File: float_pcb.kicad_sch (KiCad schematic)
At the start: 74 parts, among them J1 Switch, J2 Conn_01x04, J3 USB_C, J4 Conn_01x03, J5 I2C, J6 Light, J7 Batt, J9 I2C, Q1 AO3400A, Q2 AO3400A, U1 TPSM863252, U2 TPSM863252, U3 USBLC6-2SC6, U4 ESP32-S3-WROOM-1, U5 USBLC6-4SC6, U6 USBLC6-4SC6

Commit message: More progress on V4
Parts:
- U4: value ESP32-S3-WROOM-1 -> ESP32-S3-WROOM-1U
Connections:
- net USBC_D+: now reaches J3.A6 (D+), J3.B6 (D+), U3.6 (I/O1)
- net USBC_D-: now reaches J3.A7 (D-), J3.B7 (D-), U3.4 (I/O2)
- net ESP32_D-: now reaches U3.3 (I/O2), U4.13 (USB_D-)
- net ESP32_D+: now reaches U3.1 (I/O1), U4.14 (USB_D+)
- net VBUS renamed VBUS_USB
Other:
- note added: "GPIO47/48 valid only for non-R16V module variants"
- note added: "USBC"
- moved on the sheet: BOOT1, J3, R10, R11, TP9, U3

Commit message: V4
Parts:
- removed J2: Conn_01x04, Connector_PinHeader_2.54mm:PinHeader_1x04_P2.54mm_Vertical, symbol Connector_Generic:Conn_01x04
- removed LS1: AT-1127-ST-2-R, buzzer:XDCR_AT-1127-ST-2-R, symbol Buzzer:AT-1127-ST-2-R
- removed Q2: AO3400A, Package_TO_SOT_SMD:SOT-23, symbol Transistor_FET:AO3400A
- removed R26: TBD, Resistor_SMD:R_0603_1608Metric, symbol Device:R
- removed U3: USBLC6-2SC6, Package_TO_SOT_SMD:SOT-23-6, symbol Power_Protection:USBLC6-2SC6
- removed U5, U6: USBLC6-4SC6, Package_TO_SOT_SMD:SOT-23-6, symbol Power_Protection:USBLC6-4SC6
- added D4, D5, D6: ESDS314, Package_TO_SOT_SMD:SOT-23-5, symbol float_pcb_symbols:ESDS314
- added H4: MH, MountingHole:MountingHole_2.2mm_M2, symbol Mechanical:MountingHole
- added J2: Conn_01x05, Connector_PinHeader_2.54mm:PinHeader_1x05_P2.54mm_Vertical, symbol Connector_Generic:Conn_01x05
- added LS1: CPT-9019A-SMT-TR, buzzer:CPT-9019A_CUD, symbol Buzzer:CPT-9019A-SMT-TR
- R20: value 10k -> 1k
- TP7: value SDA2 -> SDA1
- renumbered R25 to R22, R22 to R25
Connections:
- net ESP32_D+ is gone; now on net USBC_D+: U4.14 (USB_D+)
- net ESP32_D- is gone; now on net USBC_D-: U4.13 (USB_D-)
- net BUZZER: now also R20.1; no longer R20.2
- net GND: now also R17.1, D4.2 (GND), D5.2 (GND), D6.2 (GND), J2.5 (Pin_5), LS1.2; no longer R17.2, R20.1
- net LIGHT: now also R17.2; no longer R17.1
- net MISC1: now also R25.1, U4.33 (IO40), D5.5 (IO4), J2.1 (Pin_1); no longer R22.2, U4.32 (IO39)
- net MISC2: now also R23.1, U4.34 (IO41), D5.4 (IO3), J2.2 (Pin_2); no longer R24.2, U4.31 (IO38)
- net MISC3: now also R24.2, U4.31 (IO38), D5.3 (IO2), J2.3 (Pin_3); no longer R23.1, U4.34 (IO41)
- net MISC4: now also R22.2, U4.32 (IO39), D5.1 (IO1), J2.4 (Pin_4); no longer R25.1, U4.33 (IO40)
- net SCL1: now also D6.1 (IO1)
- net SCL2: now also D6.4 (IO3)
- net SDA1: now also D6.3 (IO2)
- net SDA2: now also D6.5 (IO4)
- net USBC_D+: now also D4.3 (IO2)
- net USBC_D-: now also D4.1 (IO1)
- net VBUS_USB renamed USB_VBUS
- new net: LS1.1, R20.2
- no-connect marks 26 -> 28
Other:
- moved on the sheet: H1, H2, H3, R17, R20, R22, R23, R24, R25

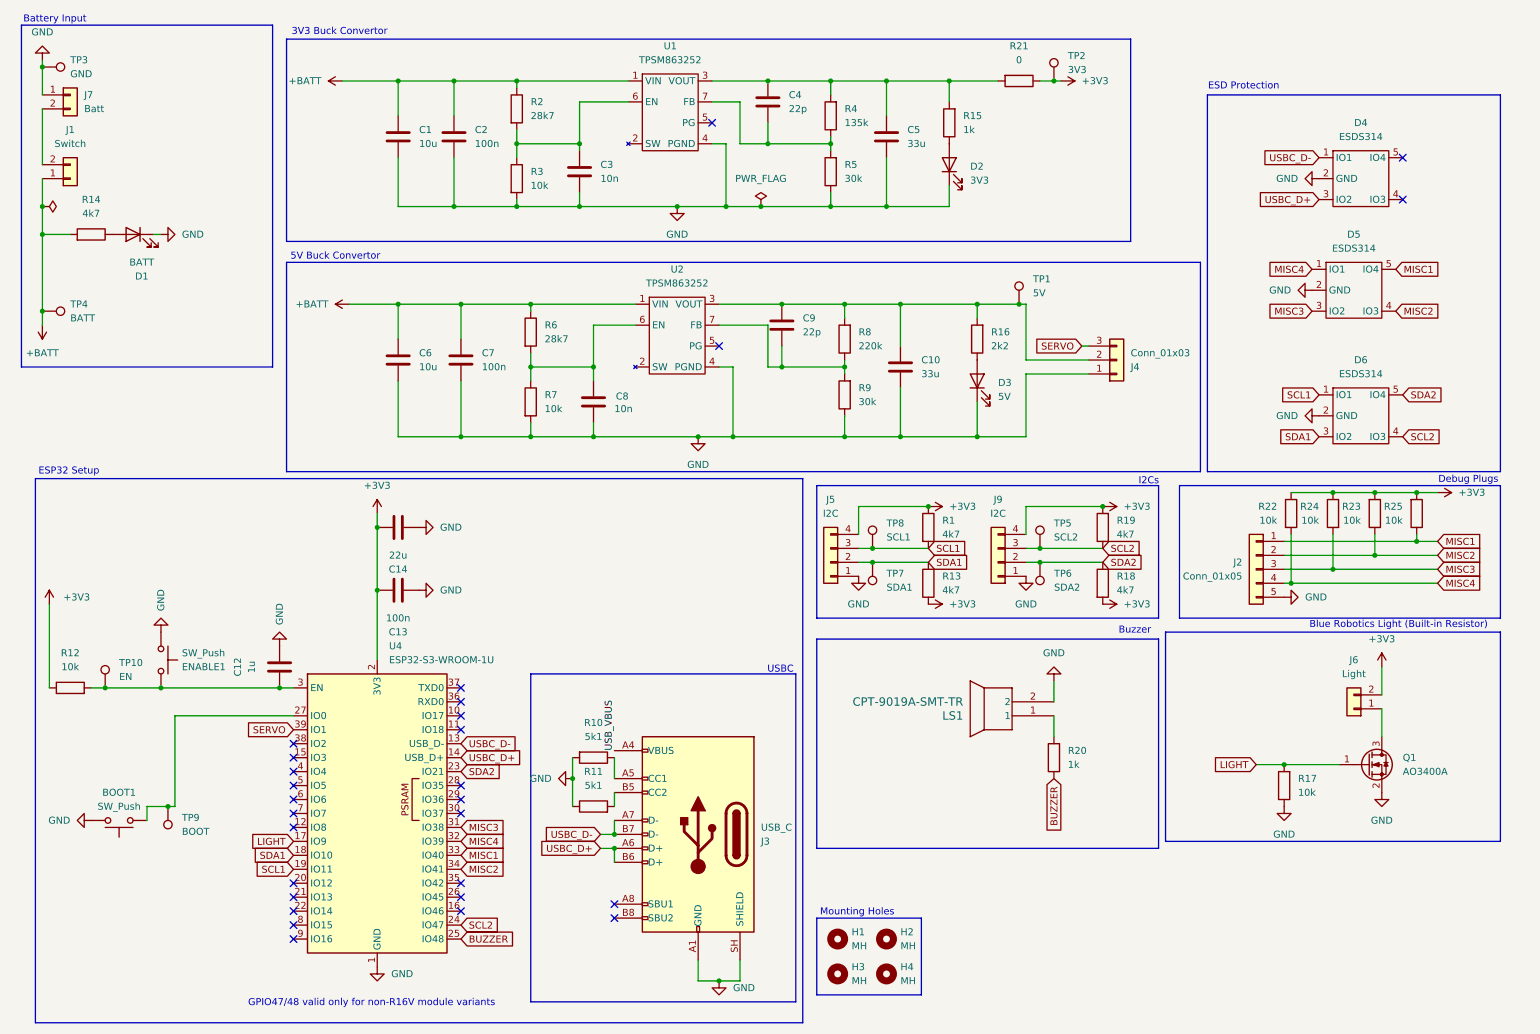
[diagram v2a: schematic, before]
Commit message: Starting V5: new 33uf new servo cap, ADC and voltage dividor
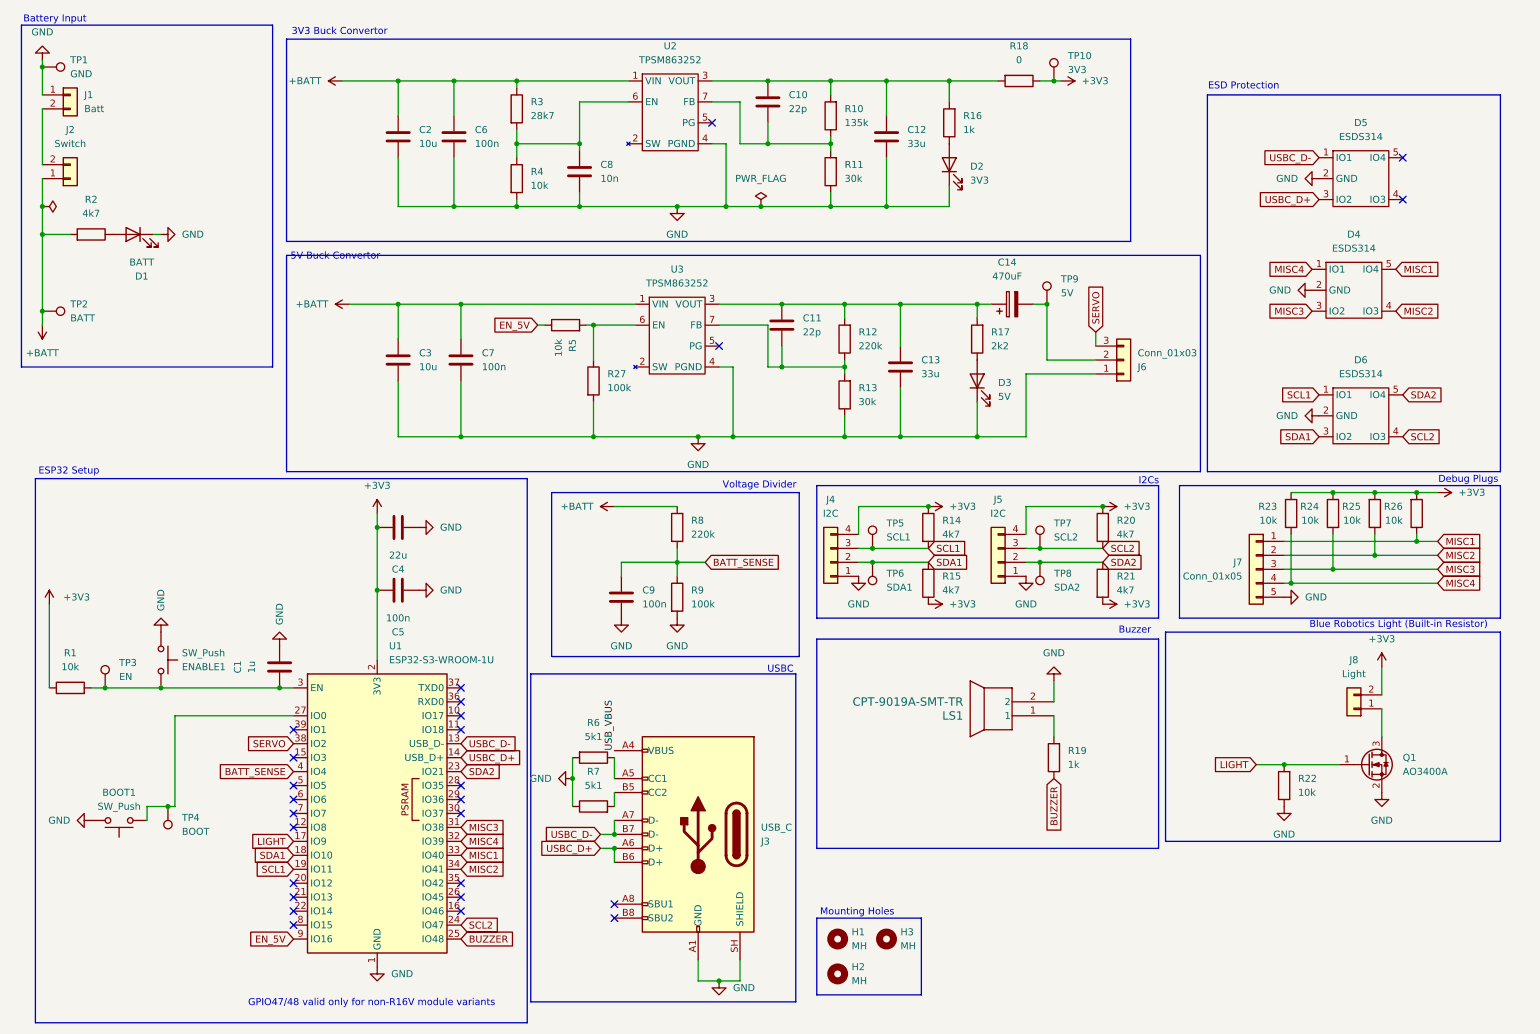
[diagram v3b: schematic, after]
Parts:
- removed C8: 10n, Capacitor_SMD:C_0603_1608Metric, symbol Device:C
- removed H4: MH, MountingHole:MountingHole_2.2mm_M2, symbol Mechanical:MountingHole
- removed R6: 28k7, Resistor_SMD:R_0603_1608Metric, symbol Device:R
- removed R7: 10k, Resistor_SMD:R_0603_1608Metric, symbol Device:R
- removed TP1: 5V, TestPoint:TestPoint_Pad_D1.5mm, symbol Connector:TestPoint
- added C14: 470uF, Capacitor_THT:CP_Radial_D6.3mm_P2.50mm, symbol Device:C_Polarized
- added C9: 100n, Capacitor_SMD:C_0603_1608Metric, symbol Device:C
- added R27, R9: 100k, Resistor_SMD:R_0603_1608Metric, symbol Device:R
- added R5: 10k, Resistor_SMD:R_0603_1608Metric, symbol Device:R
- added R8: 220k, Resistor_SMD:R_0603_1608Metric, symbol Device:R
- added TP9: 5V, TestPoint:TestPoint_Pad_D1.5mm, symbol Connector:TestPoint
- C12: renamed from C5; footprint Capacitor_SMD:C_0805_2012Metric -> Capacitor_SMD:C_1206_3216Metric
- C13: renamed from C10; footprint Capacitor_SMD:C_0805_2012Metric -> Capacitor_SMD:C_1206_3216Metric
- renumbered C12 to C1, C4 to C10, C9 to C11, C1 to C2, C6 to C3, C14 to C4, C13 to C5, C2 to C6, C3 to C8, D5 to D4, D4 to D5, H3 to H2, H2 to H3, J7 to J1, J1 to J2, J5 to J4, J9 to J5, J4 to J6, J2 to J7, J6 to J8, R12 to R1, R4 to R10, R5 to R11, R8 to R12, R9 to R13, R1 to R14, R13 to R15, R15 to R16, R16 to R17, R21 to R18, R20 to R19, R14 to R2, R19 to R20, R18 to R21, R17 to R22, R22 to R23, R23 to R25, R25 to R26, R2 to R3, R3 to R4, R10 to R6, R11 to R7, TP3 to TP1, TP2 to TP10, TP4 to TP2, TP10 to TP3, TP9 to TP4, TP8 to TP5, TP7 to TP6, TP5 to TP7, TP6 to TP8, U4 to U1, U1 to U2, U2 to U3
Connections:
- net +BATT: now also R8.1
- net GND: now also C9.2, R27.2, R9.2
- net SERVO: now also U1.38 (IO2); no longer U1.39 (IO1)
- net at C11.1, C13.2, R12.2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: now also C14.1; no longer J6.2 (Pin_2)
- net at U3.6 (EN): now also R27.1, R5.2
- net BATT_SENSE: now reaches U1.4 (IO4)
- net BATT_SENSE: now also C9.1, R8.2, R9.1
- net EN_5V: now reaches U1.9 (IO16)
- net EN_5V: now also R5.1
- new net: C14.2, J6.2 (Pin_2), TP9.1
- no-connect marks 28 -> 26
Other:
- note added: "Voltage Divider"
- moved on the sheet: J6

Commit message: Continuing Test Pads and some placement things
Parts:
- added TP11: BATT_ADC, TestPoint:TestPoint_Pad_D1.5mm, symbol Connector:TestPoint
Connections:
- net BATT_SENSE: now also TP11.1
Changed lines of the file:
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@@
 	(text "5V Buck Convertor\n"
 		(exclude_from_sim no)
-		(at 69.85 57.404 0)
+		(at 69.596 56.388 0)
 		(effects
 			(font
@@
 	)
 	(junction
+		(at 121.92 113.03)
+		(diameter 0)
+		(color 0 0 0 0)
+	)
+	(junction
 		(at 114.3 36.83)
 		(diameter 0)
@@
 	(wire
 		(pts
+			(xy 118.11 113.03) (xy 121.92 113.03)
+		)
+		(stroke
+			(width 0)
+			(type default)
+		)
+	)
+	(wire
+		(pts
 			(xy 81.28 90.17) (xy 92.71 90.17)
 		)
@@
 					(unit 1)
 				)
+			)
+		)
+	)
+	(symbol
+		(lib_id "Connector:TestPoint")
+		(at 118.11 113.03 0)
+		(unit 1)
+		(body_style 1)
+		(exclude_from_sim no)
+		(in_bom yes)
+		(on_board yes)
+		(in_pos_files yes)
+		(dnp no)
+		(fields_autoplaced yes)
+		(property "Reference" "TP11"
+			(at 120.65 108.4579 0)
+			(show_name no)
+			(do_not_autoplace no)
+			(effects
+				(font
+					(size 1.27 1.27)
+				)
+				(justify left)
+			)
+		)
+		(property "Value" "BATT_ADC"
+			(at 120.65 110.9979 0)
+			(show_name no)
+			(do_not_autoplace no)
+			(effects
+				(font
+					(size 1.27 1.27)
+				)
+				(justify left)
+			)
+		)
+		(property "Footprint" "TestPoint:TestPoint_Pad_D1.5mm"
+			(at 123.19 113.03 0)
+			(hide yes)
+			(show_name no)
+			(do_not_autoplace no)
+			(effects
+				(font
+					(size 1.27 1.27)
+				)
+			)
+		)
+		(property "Datasheet" ""
+			(at 123.19 113.03 0)
+			(hide yes)
+			(show_name no)
+			(do_not_autoplace no)
+			(effects
+				(font
+					(size 1.27 1.27)
+				)
+			)
+		)
+		(property "Description" "test point"
+			(at 118.11 113.03 0)
+			(hide yes)
+			(show_name no)
+			(do_not_autoplace no)
+			(effects
+				(font
+					(size 1.27 1.27)
+				)
+			)
+		)
+		(pin "1"
+		)
+		(instances
+			(project "float_pcb"
+				(path "/c862e882-4741-4de1-b296-17adfea7dce3"
+					(reference "TP11")
+					(unit 1)
+				)

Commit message: V5: Sent for production!
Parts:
- C14: value 470uF -> 470u
- renumbered R7 to R10, R10 to R11, R11 to R12, R12 to R13, R13 to R14, R14 to R15, R15 to R16, R16 to R17, R17 to R18, R18 to R19, R19 to R20, R20 to R21, R21 to R22, R22 to R23, R23 to R24, R24 to R25, R25 to R26, R26 to R27, R27 to R6, R8 to R7, R9 to R8, R6 to R9, TP8 to TP10, TP10 to TP11, TP11 to TP5, TP5 to TP6, TP6 to TP7, TP9 to TP8, TP7 to TP9
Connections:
- net BUZZER: now also R20.2; no longer R20.1
- net GND: now also C14.2
- net at C11.1, C13.2, C14.1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: now also J6.2 (Pin_2), TP8.1
- net at LS1.1: now also R20.1; no longer R20.2
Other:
- moved on the sheet: C4, C5, D3, J3, LS1, R10, R18, R20, R9, TP8
